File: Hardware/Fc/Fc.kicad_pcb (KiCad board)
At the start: 2 copper layers, 90 parts, among them J1 PWR, J2 Raspberry_Pi_2_3, U1 STM32F407VGTx, U2 INA219AIDCNR, U3 MPU-6000

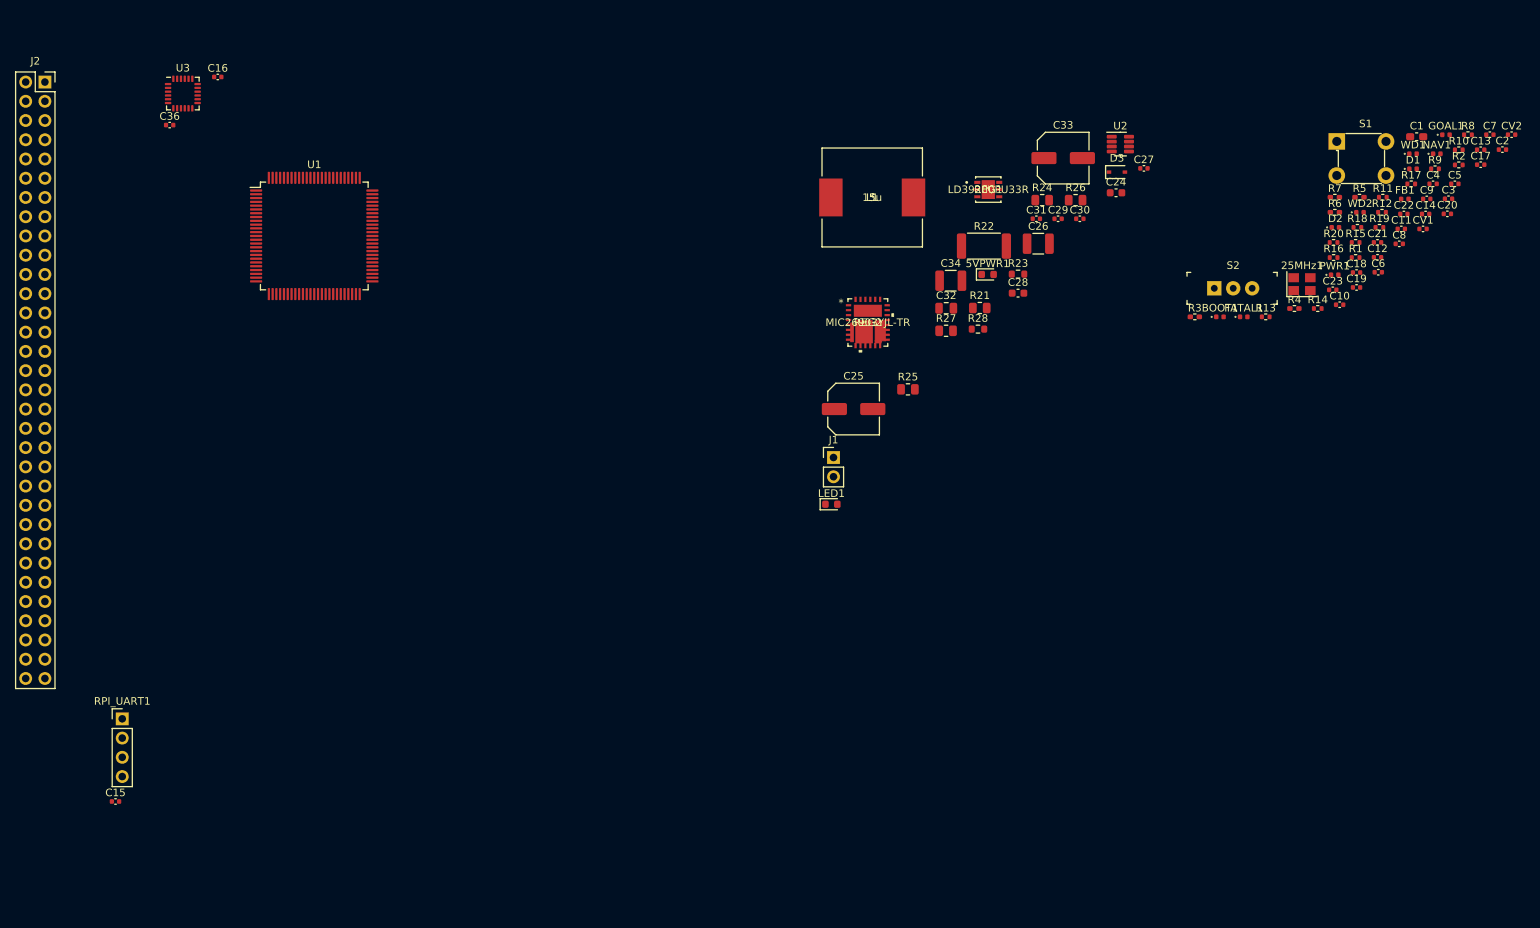
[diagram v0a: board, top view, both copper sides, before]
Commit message: Building with new libcamera updates
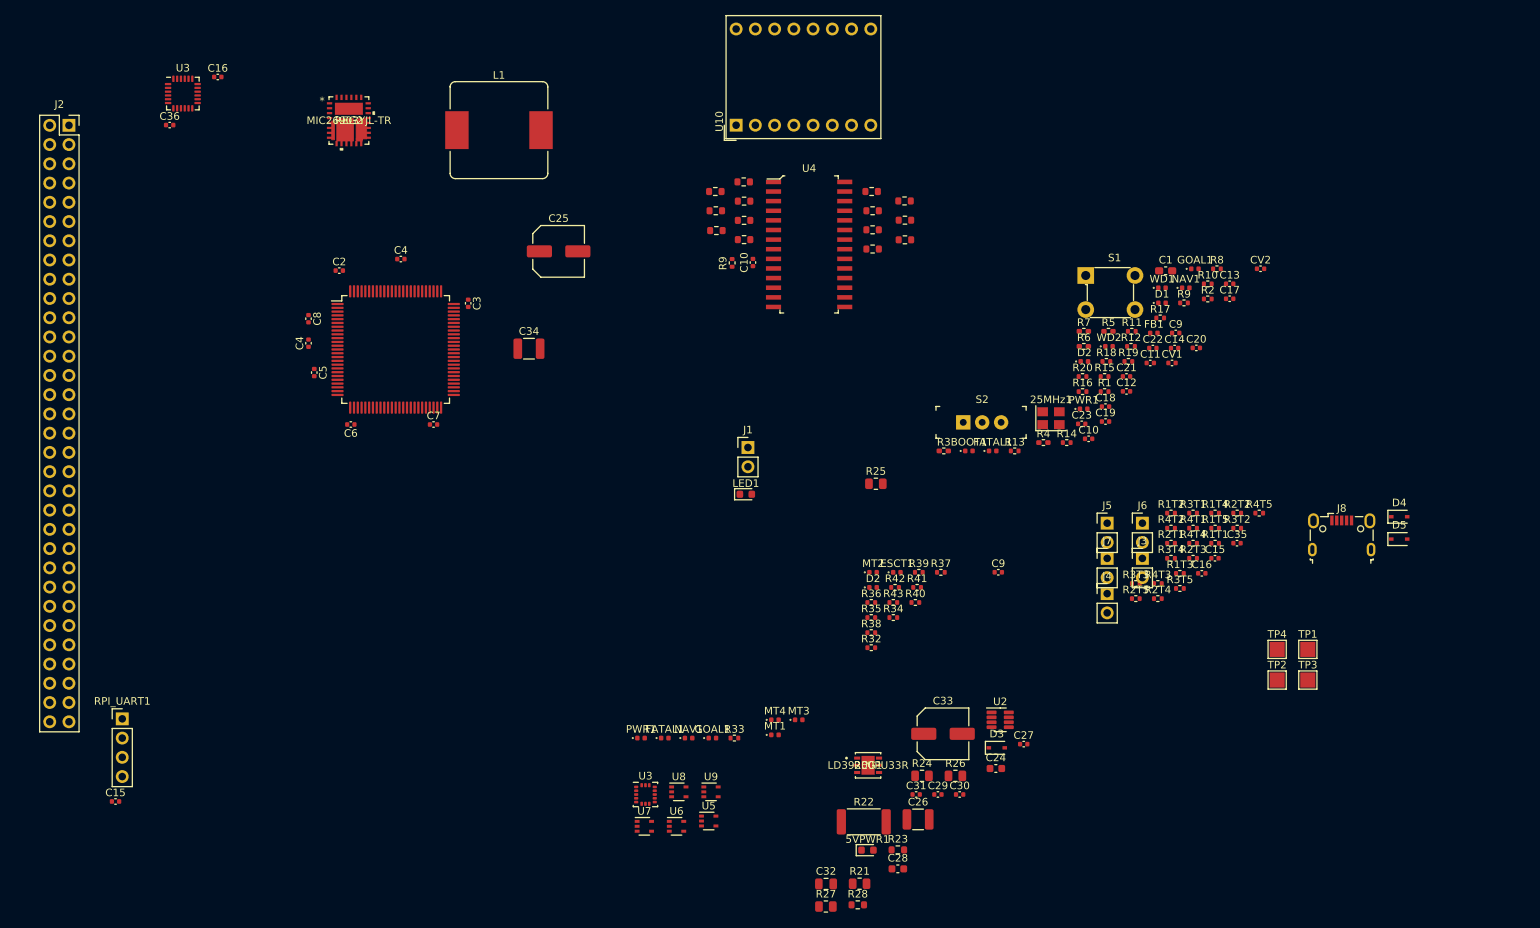
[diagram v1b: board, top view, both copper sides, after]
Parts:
- added C10: 0.1u, Capacitor_SMD:C_0402_1005Metric, F.Cu at (136.7, 69.5)
- added C15: 0.1u, Capacitor_SMD:C_0402_1005Metric, F.Cu at (197.6, 108.6)
- added C16: 2u2, Capacitor_SMD:C_0402_1005Metric, F.Cu at (195.9, 110.6)
- added C35: 0.1u, Capacitor_SMD:C_0402_1005Metric, F.Cu at (200.6, 106.6)
- added C4: 100n, Capacitor_SMD:C_0402_1005Metric, F.Cu at (90.2, 69.1)
- added C9: 1u, Capacitor_SMD:C_0402_1005Metric, F.Cu at (169.0, 110.4)
- added D2: BAT, LED_SMD:LED_0402_1005Metric, F.Cu at (152.5, 112.4)
- added D4: SD103AWS, Diode_SMD:D_SOD-323, F.Cu at (222.0, 103.1)
- added D5: SD103AWS, Diode_SMD:D_SOD-323, F.Cu at (222.0, 106.1)
- added ESCT1: R, LED_SMD:LED_0402_1005Metric, F.Cu at (155.6, 110.4)
- added FATAL1: R, LED_SMD:LED_0402_1005Metric, F.Cu at (125.0, 132.3)
- added GOAL1: G, LED_SMD:LED_0402_1005Metric, F.Cu at (131.3, 132.3)
- added J3: Conn_01x02_Male, Connector_PinHeader_2.54mm:PinHeader_1x02_P2.54mm_Vertical, F.Cu at (188.1, 108.6)
- added J4: Conn_01x02_Male, Connector_PinHeader_2.54mm:PinHeader_1x02_P2.54mm_Vertical, F.Cu at (183.4, 113.3)
- added J5: Conn_01x02_Male, Connector_PinHeader_2.54mm:PinHeader_1x02_P2.54mm_Vertical, F.Cu at (183.4, 104.0)
- added J6: Conn_01x02_Male, Connector_PinHeader_2.54mm:PinHeader_1x02_P2.54mm_Vertical, F.Cu at (188.1, 104.0)
- added J7: Conn_01x02_Male, Connector_PinHeader_2.54mm:PinHeader_1x02_P2.54mm_Vertical, F.Cu at (183.4, 108.6)
- added J8: USB_B_Micro, Connector_USB:USB_Micro-B_Wuerth_629105150521, F.Cu at (214.4, 105.5)
- added MT1: R, LED_SMD:LED_0402_1005Metric, F.Cu at (139.6, 131.9)
- added MT2: R, LED_SMD:LED_0402_1005Metric, F.Cu at (152.5, 110.4)
- added MT3: R, LED_SMD:LED_0402_1005Metric, F.Cu at (142.7, 129.9)
- added MT4: R, LED_SMD:LED_0402_1005Metric, F.Cu at (139.6, 129.9)
- added NAV1: G, LED_SMD:LED_0402_1005Metric, F.Cu at (128.2, 132.3)
- added PWR1: R, LED_SMD:LED_0402_1005Metric, F.Cu at (121.9, 132.3)
- added R10: 150R, Resistor_SMD:R_0603_1608Metric, F.Cu at (135.4, 58.9)
- added R11: 150R, Resistor_SMD:R_0603_1608Metric, F.Cu at (131.7, 60.2)
- added R12: 150R, Resistor_SMD:R_0603_1608Metric, F.Cu at (135.5, 61.4)
- added R13: 150R, Resistor_SMD:R_0603_1608Metric, F.Cu at (131.7, 62.7)
- added R14: 150R, Resistor_SMD:R_0603_1608Metric, F.Cu at (135.5, 64.0)
- added R15: 150R, Resistor_SMD:R_0603_1608Metric, F.Cu at (131.8, 65.3)
- added R16: 150R, Resistor_SMD:R_0603_1608Metric, F.Cu at (135.5, 66.5)
- added R17: 150R, Resistor_SMD:R_0603_1608Metric, F.Cu at (152.5, 67.8)
- added R18: 150R, Resistor_SMD:R_0603_1608Metric, F.Cu at (156.7, 66.5)
- added R19: 150R, Resistor_SMD:R_0603_1608Metric, F.Cu at (152.5, 65.2)
- added R1T1: 6k02, Resistor_SMD:R_0402_1005Metric, F.Cu at (197.7, 106.6)
- added R1T2: 6k02, Resistor_SMD:R_0402_1005Metric, F.Cu at (191.8, 102.6)
- added R1T3: 6k02, Resistor_SMD:R_0402_1005Metric, F.Cu at (193.0, 110.6)
- added R1T4: 6k02, Resistor_SMD:R_0402_1005Metric, F.Cu at (197.7, 102.6)
- added R1T5: 6k02, Resistor_SMD:R_0402_1005Metric, F.Cu at (197.7, 104.6)
- added R20: 150R, Resistor_SMD:R_0603_1608Metric, F.Cu at (156.7, 64.0)
- added R29: 150R, Resistor_SMD:R_0603_1608Metric, F.Cu at (152.5, 62.7)
- added R2T1: 7k7, Resistor_SMD:R_0402_1005Metric, F.Cu at (191.8, 106.6)
- added R2T2: 7k7, Resistor_SMD:R_0402_1005Metric, F.Cu at (200.6, 102.6)
- added R2T3: 7k7, Resistor_SMD:R_0402_1005Metric, F.Cu at (194.8, 108.6)
- added R2T4: 7k7, Resistor_SMD:R_0402_1005Metric, F.Cu at (190.1, 113.9)
- added R2T5: 7k7, Resistor_SMD:R_0402_1005Metric, F.Cu at (187.2, 113.9)
- added R30: 150R, Resistor_SMD:R_0603_1608Metric, F.Cu at (156.7, 61.4)
- added R31: 150R, Resistor_SMD:R_0603_1608Metric, F.Cu at (152.3, 60.2)
- added R32: 1k, Resistor_SMD:R_0402_1005Metric, F.Cu at (152.3, 120.4)
- added R33: 2k2, Resistor_SMD:R_0402_1005Metric, F.Cu at (134.2, 132.3)
- added R34: 1k, Resistor_SMD:R_0402_1005Metric, F.Cu at (155.2, 116.4)
- added R35: 1k, Resistor_SMD:R_0402_1005Metric, F.Cu at (152.3, 116.4)
- added R36: 2k2, Resistor_SMD:R_0402_1005Metric, F.Cu at (152.3, 114.4)
- added R37: 1k, Resistor_SMD:R_0402_1005Metric, F.Cu at (161.5, 110.4)
- added R38: 1k, Resistor_SMD:R_0402_1005Metric, F.Cu at (152.3, 118.4)
- added R39: 1k, Resistor_SMD:R_0402_1005Metric, F.Cu at (158.6, 110.4)
- added R3T1: 7k7, Resistor_SMD:R_0402_1005Metric, F.Cu at (194.8, 102.6)
- added R3T2: 7k7, Resistor_SMD:R_0402_1005Metric, F.Cu at (200.6, 104.6)
- added R3T3: 7k7, Resistor_SMD:R_0402_1005Metric, F.Cu at (187.2, 111.9)
- added R3T4: 7k7, Resistor_SMD:R_0402_1005Metric, F.Cu at (191.8, 108.6)
- added R3T5: 7k7, Resistor_SMD:R_0402_1005Metric, F.Cu at (193.0, 112.6)
- added R40: 1k, Resistor_SMD:R_0402_1005Metric, F.Cu at (158.1, 114.4)
- added R41: 2k2, Resistor_SMD:R_0402_1005Metric, F.Cu at (158.3, 112.4)
- added R42: 2k2, Resistor_SMD:R_0402_1005Metric, F.Cu at (155.4, 112.4)
- added R43: 1k, Resistor_SMD:R_0402_1005Metric, F.Cu at (155.2, 114.4)
- added R4T1: 1k5, Resistor_SMD:R_0402_1005Metric, F.Cu at (194.8, 104.6)
- added R4T2: 1k5, Resistor_SMD:R_0402_1005Metric, F.Cu at (191.8, 104.6)
- added R4T3: 1k5, Resistor_SMD:R_0402_1005Metric, F.Cu at (190.1, 111.9)
- added R4T4: 1k5, Resistor_SMD:R_0402_1005Metric, F.Cu at (194.8, 106.6)
- added R4T5: 1k5, Resistor_SMD:R_0402_1005Metric, F.Cu at (203.5, 102.6)
- added R9: 10k, Resistor_SMD:R_0402_1005Metric, F.Cu at (133.9, 69.6)
- added TP1: VBAT, TestPoint:TestPoint_Pad_2.0x2.0mm, F.Cu at (209.9, 120.6)
- added TP2: +5V, TestPoint:TestPoint_Pad_2.0x2.0mm, F.Cu at (205.9, 124.7)
- added TP3: +3V3, TestPoint:TestPoint_Pad_2.0x2.0mm, F.Cu at (209.9, 124.7)
- added TP4: GND, TestPoint:TestPoint_Pad_2.0x2.0mm, F.Cu at (205.9, 120.6)
- added U10: DA04-11SURKWA, Display_7Segment:DA04-11SURKWA, F.Cu at (134.4, 51.4)
- added U3: ICM-20602, Package_LGA:LGA-16_3x3mm_P0.5mm_LayoutBorder3x5y, F.Cu at (122.5, 139.8)
- added U4: MCP23017-E_SO, digikey-footprints:SOIC-28_W7.5mm, F.Cu at (144.1, 67.2)
- added U5: TLV9001IDCK, Package_TO_SOT_SMD:SOT-353_SC-70-5, F.Cu at (130.8, 143.3)
- added U6: TLV9001IDCK, Package_TO_SOT_SMD:SOT-353_SC-70-5, F.Cu at (126.6, 144.0)
- added U7: TLV9001IDCK, Package_TO_SOT_SMD:SOT-353_SC-70-5, F.Cu at (122.3, 144.0)
- added U8: TLV9001IDCK, Package_TO_SOT_SMD:SOT-353_SC-70-5, F.Cu at (126.9, 139.4)
- added U9: TLV9001IDCK, Package_TO_SOT_SMD:SOT-353_SC-70-5, F.Cu at (131.1, 139.4)
- FB1: value FerriteBead_Small -> 120R
- L1: footprint cad:SRP1265A-470M -> Inductor_SMD:L_Bourns_SRP1245A
- moved C2 154.4 mm to (82.0, 70.6)
- moved C5 152.6 mm to (78.7, 84.1), turned to -90 degrees
- moved C4 150.0 mm to (78.0, 80.2), turned to 90 degrees
- moved C7 144.6 mm to (94.5, 90.9)
- moved C8 144.3 mm to (78.0, 77.0), turned to -90 degrees
- moved C6 137.1 mm to (83.6, 90.9), turned to 180 degrees
- moved C3 130.2 mm to (99.1, 74.9), turned to -90 degrees
- moved C32 77.6 mm to (146.3, 151.6)
- moved D3 77.6 mm to (168.8, 133.6)
- moved R21 77.6 mm to (150.7, 151.6)
- moved R23 77.6 mm to (155.8, 147.1)
- moved 5VPWR1 77.6 mm to (151.8, 147.1)
- moved C24 77.6 mm to (168.7, 136.3)
- moved C26 77.6 mm to (158.5, 143.1)
- moved C27 77.6 mm to (172.4, 133.1)
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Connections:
- 5VPWR1 pad 2: +5V -> 5VBAT
- C32 pad 1: +5V -> 5VBAT
- C33 pad 1: +5V -> 5VBAT
- C34 pad 1: +5V -> 5VBAT
- L1 pad 2: +5V -> 5VBAT
- R26 pad 1: +5V -> 5VBAT
- U1 pad 23: ADC1_IN0 -> THRM1
- U1 pad 24: ADC2_IN1 -> THRM2
- U1 pad 25: ADC3_IN2 -> THRM3
- U1 pad 34: unconnected-(U1-Pad34) -> THRM5
- U1 pad 35: unconnected-(U1-Pad35) -> THRM4
- U1 pad 38: LED8 -> unconnected-(U1-Pad38)
- U1 pad 45: TIM1_CH4 -> unconnected-(U1-Pad45)
- U1 pad 68: USB_OTG_FS_VBUS -> unconnected-(U1-Pad68)
- U1 pad 69: USB_OTG_FS_ID -> unconnected-(U1-Pad69)
- U1 pad 7: unconnected-(U1-Pad7) -> LED8
- U1 pad 70: USB_OTG_FS_DM -> USB_D-
- U1 pad 71: USB_OTG_FS_DP -> USB_D+
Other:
- copper layers 2 -> 4
